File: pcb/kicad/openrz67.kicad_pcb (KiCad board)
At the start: 2 copper layers, 48 x 22 mm, 59 parts, among them U1 ESP32-C3FH4, U3 LGS5500EP, U4 S4B-XH-A(LF)(SN), U5 TLP172GM, U6 TLP172GM, X1 40MHz, X2 32.768kHz

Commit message: Update rev 2 PCB layout
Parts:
- BAT1: value S2B-PH-SM4-TB(LF)(SN) -> B2B-PH-K-S(LF)(SN); footprint openrz67:CONN-SMD_P2.00_S2B-PH-SM4-TB-LF-SN -> openrz67:CONN-TH_B2B-PH-K-S; moved to F.Cu
- moved BAT1 6.34 mm to (123.3, 94.8), turned to 90 degrees
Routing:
- net BAT+: track 17.1 -> 14.2 mm, vias 1 -> 0
- net GND: vias 103 -> 108

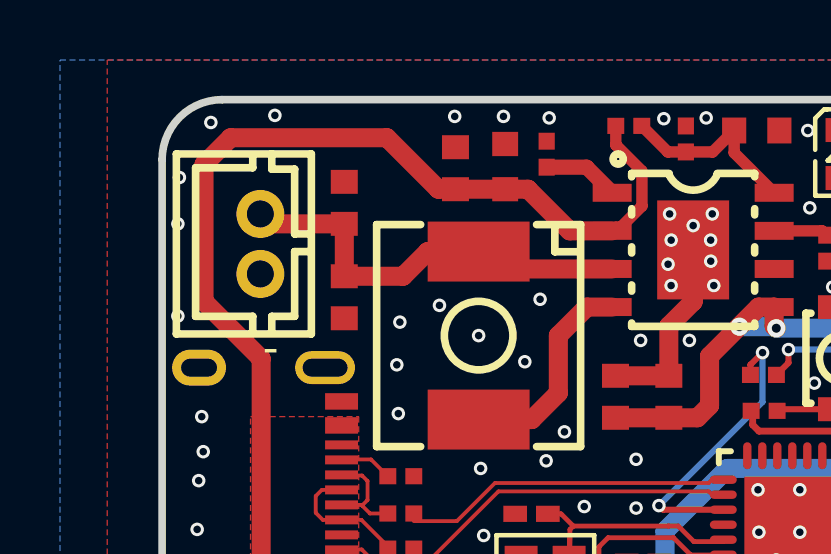
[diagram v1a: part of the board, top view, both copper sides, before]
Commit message: Revert "Update rev 2 PCB layout"
This reverts commit d763081e84975234f8d2c617ac684d1041c5a9e0.
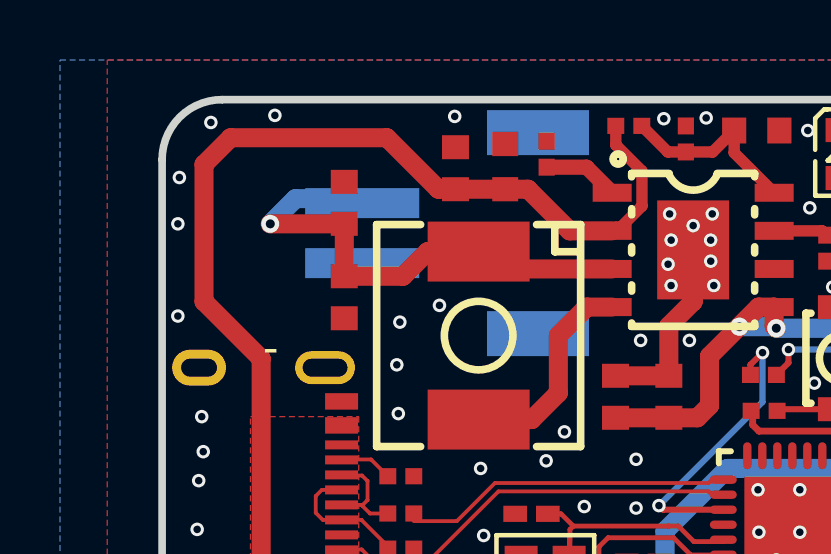
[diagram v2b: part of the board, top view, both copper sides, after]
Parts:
- BAT1: value B2B-PH-K-S(LF)(SN) -> S2B-PH-SM4-TB(LF)(SN); footprint openrz67:CONN-TH_B2B-PH-K-S -> openrz67:CONN-SMD_P2.00_S2B-PH-SM4-TB-LF-SN; moved to B.Cu
- moved BAT1 6.34 mm to (129.6, 94.5), turned to -90 degrees
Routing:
- net BAT+: track 14.2 -> 17.1 mm, vias 0 -> 1
- net GND: vias 108 -> 103
